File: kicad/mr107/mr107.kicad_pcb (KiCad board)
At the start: 2 copper layers, 35.8 x 70.1 mm, 70 parts, among them J1 USB_A, J10 L-KLS12, J2 gnd, J3 mosi, J4 miso, J5 sclk, J6 reset, J7 gnd, J8 gnd, J9 PW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

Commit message: изменено:      AVR/mr107_/mr107_.ino 	новый файл:    kicad/mr107/bom/ibom.html 	изменено:      kicad/mr107/gerber/Border.gbr 	изменено:      kicad/mr107/gerber/Bottom.gbr 	изменено:      kicad/mr107/gerber/MaskBottom.gbr 	изменено:      kicad/mr107/gerber/MaskTop.gbr 	изменено:      kicad/mr107/gerber/NCData.drl 	изменено:      kicad/mr107/gerber/Top.gbr 	изменено:      kicad/mr107/gerber/mk-gerber.sh 	изменено:      kicad/mr107/gerber/mk-gerber.sh~ 	изменено:      kicad/mr107/gerber/mr107-job.gbrjob 	изменено:      kicad/mr107/gerber/mr107.zip 	удалено:       kicad/mr107/mr107-backups/mr107-2023-12-05_182551.zip 	удалено:       kicad/mr107/mr107-backups/mr107-2023-12-05_183551.zip 	удалено:       kicad/mr107/mr107-backups/mr107-2023-12-05_184551.zip 	удалено:       kicad/mr107/mr107-backups/mr107-2023-12-05_190040.zip 	удалено:       kicad/mr107/mr107-backups/mr107-2023-12-06_163733.zip 	удалено:       kicad/mr107/mr107-backups/mr107-2023-12-06_164916.zip 	удалено:       kicad/mr107/mr107-backups/mr107-2023-12-06_165817.zip 	удалено:       kicad/mr107/mr107-backups/mr107-2023-12-06_185613.zip 	удалено:       kicad/mr107/mr107-backups/mr107-2023-12-06_190115.zip 	удалено:       kicad/mr107/mr107-backups/mr107-2023-12-07_163716.zip 	удалено:       kicad/mr107/mr107-backups/mr107-2023-12-07_164901.zip 	удалено:       kicad/mr107/mr107-backups/mr107-2023-12-10_204652.zip 	удалено:       kicad/mr107/mr107-backups/mr107-2023-12-12_102834.zip 	изменено:      kicad/mr107/mr107.kicad_pcb 	изменено:      kicad/mr107/mr107.kicad_prl 	изменено:      kicad/mr107/mr107.kicad_sch
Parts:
- C1, C10, C17, C7, C9: value C -> 10u
- C11, C12, C13, C14, C21, C22, C28, C6: value C -> 1u
- C29: value 10u -> 1n 2kV
- C8: value .1 -> 10n
- J1: value USB_A -> USBA DS1095B-R

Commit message: изменено:      kicad/mr107/bom/ibom.html 	удалено:       kicad/mr107/gerber/Border.gbr 	удалено:       kicad/mr107/gerber/Bottom.gbr 	удалено:       kicad/mr107/gerber/MaskBottom.gbr 	удалено:       kicad/mr107/gerber/MaskTop.gbr 	удалено:       kicad/mr107/gerber/NCData.drl 	удалено:       kicad/mr107/gerber/Top.gbr 	изменено:      kicad/mr107/gerber/mk-gerber.sh 	удалено:       kicad/mr107/gerber/mk-gerber.sh~ 	удалено:       kicad/mr107/gerber/mr107-job.gbrjob 	изменено:      kicad/mr107/gerber/mr107.zip 	удалено:       kicad/mr107/mr107-backups/mr107-2023-12-07_165931.zip 	удалено:       kicad/mr107/mr107-backups/mr107-2023-12-07_170641.zip 	изменено:      kicad/mr107/mr107.kicad_pcb 	изменено:      kicad/mr107/mr107.kicad_prl 	изменено:      kicad/mr107/mr107.kicad_sch 	удалено:       kicad/mr107_802.3af/mr107-backups/mr107-2023-12-09_164959.zip
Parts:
- C29: footprint Capacitor_SMD:C_0805_2012Metric -> Capacitor_SMD:C_1206_3216Metric
- moved D5 1.50 mm to (60.1, 112.3), turned to 180 degrees
- moved R11 1.06 mm to (73.8, 95.5)
- moved C4 1.05 mm to (63.2, 75.5), turned to 180 degrees
- moved R1 1.03 mm to (72.7, 95.5)
- moved C29 0.55 mm to (85.2, 99.4)
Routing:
- net Net-(D4-Pad3): track 16.4 -> 24.2 mm, vias 3 -> 0
- net Net-(D5-Pad2): track 20.9 -> 14.8 mm, vias 1 -> 0
- net passive_PoE: track 18.5 -> 23.5 mm
- net Net-(D4-Pad1): track 16.4 -> 13.9 mm
- net Net-(D5-Pad1): track 21.8 -> 20.4 mm, vias 1 -> 0
- net GND: vias 13 -> 14

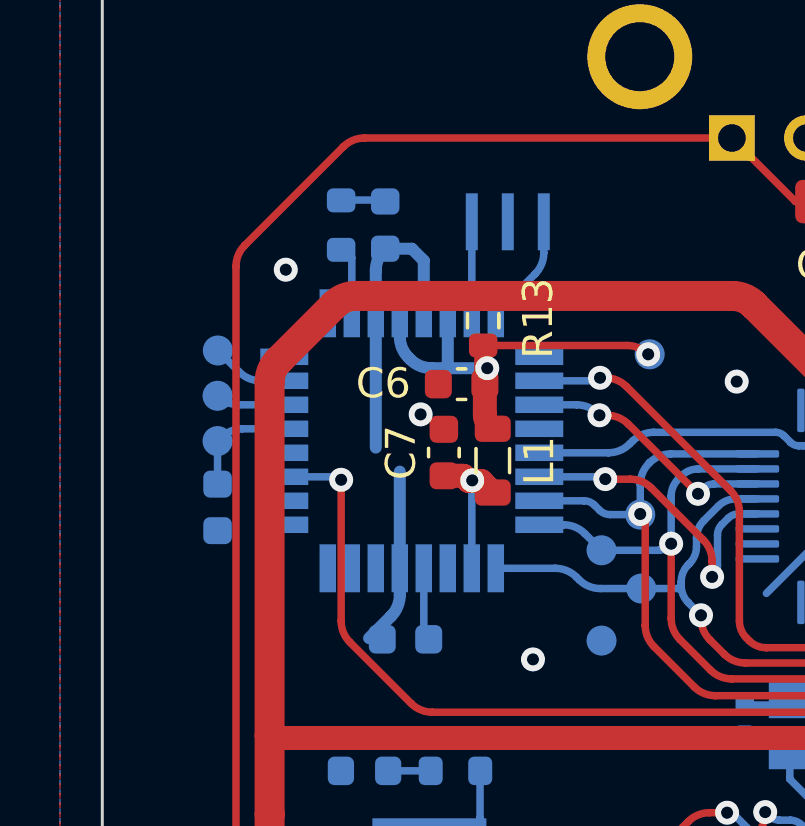
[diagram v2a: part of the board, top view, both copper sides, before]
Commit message: удалено:       kicad/mr107/mr107-backups/mr107-2023-12-12_103509.zip 	удалено:       kicad/mr107/mr107-backups/mr107-2023-12-12_104452.zip 	удалено:       kicad/mr107/mr107-backups/mr107-2023-12-12_105008.zip 	удалено:       kicad/mr107/mr107-backups/mr107-2023-12-12_105739.zip 	изменено:      kicad/mr107/mr107.kicad_pcb 	изменено:      kicad/mr107/mr107.kicad_sch
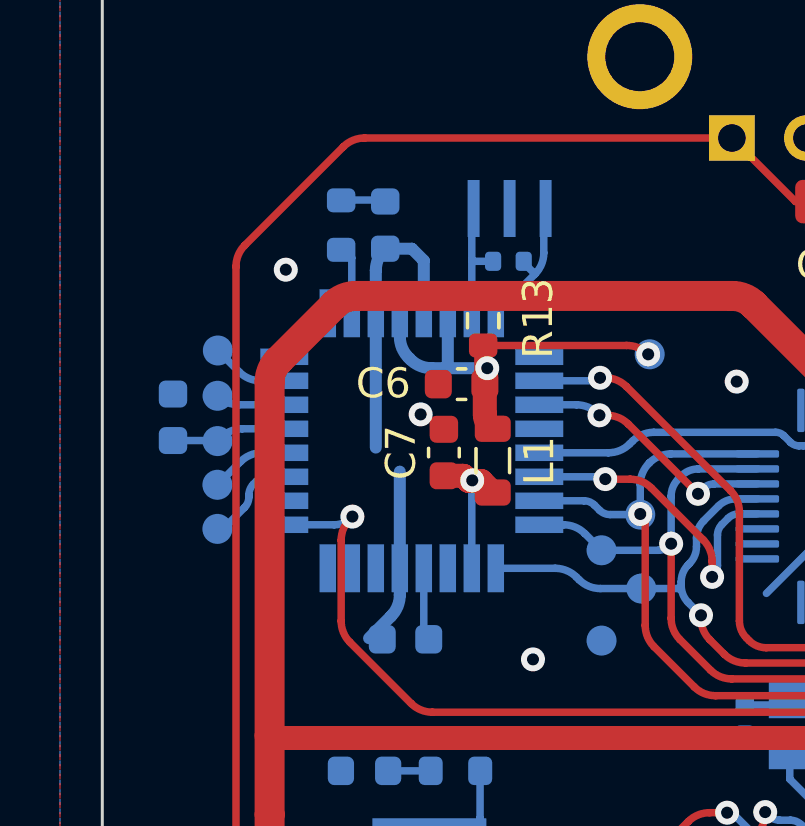
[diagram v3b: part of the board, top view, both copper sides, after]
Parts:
- added J11: mosi, lib:conn_mini, B.Cu at (56.9, 71.8)
- added J12: mosi, lib:conn_mini, B.Cu at (56.9, 70.4)
- added R17: 1M, Resistor_SMD:R_0402_1005Metric, B.Cu at (66.6, 62.9)
- J2: value gnd -> RxD
- J8: value gnd -> TxD
- moved C8 3.35 mm to (55.4, 68.1), turned to 90 degrees
- moved Y3 0.45 mm to (66.7, 61.2)
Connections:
- U2 pad 25: unconnected-(U2-Pad25) -> RST_ETH
- U2 pad 27: RST_ETH -> /sda
- U2 pad 28: unconnected-(U2-Pad28) -> /scl
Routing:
- net /sda: track 0.00 -> 3.16 mm
- net /scl: track 0.00 -> 2.62 mm
- net Net-(U2-Pad7): track 3.05 -> 3.78 mm
- net RST_ETH: track 37.6 -> 36.9 mm
- net Net-(U2-Pad8): track 3.66 -> 4.25 mm

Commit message: изменено:      kicad/mr107/gerber/mr107.zip 	изменено:      kicad/mr107/mr107.kicad_pcb 	изменено:      kicad/mr107/mr107.kicad_sch
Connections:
- U2 pad 25: RST_ETH -> unconnected-(U2-Pad25)
- U2 pad 9: unconnected-(U2-Pad9) -> RST_ETH
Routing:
- net RST_ETH: track 36.9 -> 32.9 mm
- net Net-(C6-Pad1): track 14.6 -> 15.3 mm
- net GND: vias 14 -> 15
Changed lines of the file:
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@@
   (net 54 "Net-(J1-Pad2)")
   (net 55 "Net-(J1-Pad3)")
-  (net 56 "Net-(U2-Pad7)")
-  (net 57 "Net-(U2-Pad8)")
+  (net 56 "Net-(R17-Pad1)")
+  (net 57 "Net-(R17-Pad2)")
   (net 58 "RST")
   (net 59 "Net-(C18-Pad1)")
@@
   (net 90 "/scl")
   (net 91 "Net-(D3-Pad2)")
-  (net 92 "unconnected-(U2-Pad9)")
+  (net 92 "unconnected-(U2-Pad25)")
   (net 93 "unconnected-(D4-Pad5)")
   (net 94 "Net-(D4-Pad9)")
@@
       (net 47 "Net-(C6-Pad1)") (pinfunction "VCC") (pintype "passive"))
     (pad "7" smd rect (at -4.25 -2 270) (size 1.6 0.55) (layers "B.Cu" "B.Paste" "B.Mask")
-      (net 56 "Net-(U2-Pad7)") (pinfunction "XTAL1/PB6") (pintype "bidirectional"))
+      (net 56 "Net-(R17-Pad1)") (pinfunction "XTAL1/PB6") (pintype "bidirectional"))
     (pad "8" smd rect (at -4.25 -2.8 270) (size 1.6 0.55) (layers "B.Cu" "B.Paste" "B.Mask")
-      (net 57 "Net-(U2-Pad8)") (pinfunction "XTAL2/PB7") (pintype "bidirectional"))
+      (net 57 "Net-(R17-Pad2)") (pinfunction "XTAL2/PB7") (pintype "bidirectional"))
     (pad "9" smd rect (at -2.8 -4.25 180) (size 1.6 0.55) (layers "B.Cu" "B.Paste" "B.Mask")
-      (net 92 "unconnected-(U2-Pad9)") (pinfunction "PD5") (pintype "bidirectional+no_connect"))
+      (net 84 "RST_ETH") (pinfunction "PD5") (pintype "bidirectional"))
     (pad "10" smd rect (at -2 -4.25 180) (size 1.6 0.55) (layers "B.Cu" "B.Paste" "B.Mask")
       (net 82 "SS_ETH") (pinfunction "PD6") (pintype "bidirectional"))
@@
       (net 21 "unconnected-(U2-Pad24)") (pinfunction "PC1") (pintype "bidirectional+no_connect"))
     (pad "25" smd rect (at 2.8 4.25 180) (size 1.6 0.55) (layers "B.Cu" "B.Paste" "B.Mask")
-      (net 84 "RST_ETH") (pinfunction "PC2") (pintype "bidirectional"))
+      (net 92 "unconnected-(U2-Pad25)") (pinfunction "PC2") (pintype "bidirectional+no_connect"))
     (pad "26" smd rect (at 2 4.25 180) (size 1.6 0.55) (layers "B.Cu" "B.Paste" "B.Mask")
       (net 23 "unconnected-(U2-Pad26)") (pinfunction "PC3") (pintype "bidirectional+no_connect"))
@@
     (fp_line (start -1.5 -0.3) (end -1.5 0.8) (layer "B.Fab") (width 0.1))
     (pad "1" smd rect (at -1.2 0 180) (size 0.4 1.9) (layers "B.Cu" "B.Paste" "B.Mask")
-      (net 57 "Net-(U2-Pad8)") (pinfunction "1") (pintype "passive"))
+      (net 57 "Net-(R17-Pad2)") (pinfunction "1") (pintype "passive"))
     (pad "2" smd rect (at 0 0 180) (size 0.4 1.9) (layers "B.Cu" "B.Paste" "B.Mask")
       (net 43 "GND") (pinfunction "2") (pintype "passive"))
     (pad "3" smd rect (at 1.2 0 180) (size 0.4 1.9) (layers "B.Cu" "B.Paste" "B.Mask")
-      (net 56 "Net-(U2-Pad7)") (pinfunction "3") (pintype "passive"))
+      (net 56 "Net-(R17-Pad1)") (pinfunction "3") (pintype "passive"))
     (model "${KICAD6_3DMODEL_DIR}/Crystal.3dshapes/Resonator_SMD_Murata_CSTxExxV-3Pin_3.0x1.1mm.wrl"
       (offset (xyz 0 0 0))
@@
     (fp_line (start -0.525 0.27) (end 0.525 0.27) (layer "B.Fab") (width 0.1))
     (pad "1" smd roundrect (at -0.51 0) (size 0.54 0.64) (layers "B.Cu" "B.Paste" "B.Mask") (roundrect_rratio 0.25)
-      (net 56 "Net-(U2-Pad7)") (pintype "passive"))
+      (net 56 "Net-(R17-Pad1)") (pintype "passive"))
     (pad "2" smd roundrect (at 0.51 0) (size 0.54 0.64) (layers "B.Cu" "B.Paste" "B.Mask") (roundrect_rratio 0.25)
-      (net 57 "Net-(U2-Pad8)") (pintype "passive"))
+      (net 57 "Net-(R17-Pad2)") (pintype "passive"))
     (model "${KICAD6_3DMODEL_DIR}/Resistor_SMD.3dshapes/R_0402_1005Metric.wrl"
       (offset (xyz 0 0 0))
@@
   (via (at 71.84 100.88) (size 0.8) (drill 0.4) (layers "F.Cu" "B.Cu") (free) (net 43))
   (via (at 77.02 70.64) (size 0.8) (drill 0.4) (layers "F.Cu" "B.Cu") (net 43))
+  (via (at 74.28 90.89) (size 0.8) (drill 0.4) (layers "F.Cu" "B.Cu") (free) (net 43))
   (via (at 82.33 82.91) (size 0.8) (drill 0.4) (layers "F.Cu" "B.Cu") (free) (net 43))
   (via (at 66.51 86.92) (size 0.8) (drill 0.4) (layers "F.Cu" "B.Cu") (free) (net 43))
@@
   (segment (start 78.56 80.68) (end 78.56 79.55) (width 0.25) (layer "B.Cu") (net 46))
   (segment (start 65.77 65.735) (end 65.77 66.97) (width 0.6) (layer "F.Cu") (net 47))
-  (segment (start 65.77 65.735) (end 70.560786 65.735) (width 0.25) (layer "F.Cu") (net 47))
+  (segment (start 70.015786 65) (end 66.919214 65) (width 0.25) (layer "F.Cu") (net 47))
+  (segment (start 66.212107 65.292893) (end 65.77 65.735) (width 0.25) (layer "F.Cu") (net 47))
+  (segment (start 71.27 65.84) (end 70.722893 65.292893) (width 0.25) (layer "F.Cu") (net 47))
+  (segment (start 71.27 66.03) (end 71.27 65.84) (width 0.25) (layer "F.Cu") (net 47))
   (segment (start 65.825 67.025) (end 65.825 68.040393) (width 0.8) (layer "F.Cu") (net 47))
   (segment (start 65.77 66.97) (end 65.825 67.025) (width 0.25) (layer "F.Cu") (net 47))
@@
   (via (at 65.905 66.493) (size 0.8) (drill 0.4) (layers "F.Cu" "B.Cu") (net 47))
   (via (at 71.27 66.03) (size 0.8) (drill 0.4) (layers "F.Cu" "B.Cu") (net 47))
-  (arc (start 70.560786 65.735) (mid 70.943469 65.81112) (end 71.267893 66.027893) (width 0.25) (layer "F.Cu") (net 47))
+  (arc (start 70.722893 65.292893) (mid 70.39847 65.07612) (end 70.015786 65) (width 0.25) (layer "F.Cu") (net 47))
+  (arc (start 66.212107 65.292893) (mid 66.53653 65.07612) (end 66.919214 65) (width 0.25) (layer "F.Cu") (net 47))
   (arc (start 65.971447 68.393947) (mid 65.86306 68.231735) (end 65.825 68.040393) (width 0.8) (layer "F.Cu") (net 47))
   (segment (start 64.555 66.493) (end 65.905 66.493) (width 0.4) (layer "B.Cu") (net 47))
@@
   (segment (start 79.201447 81.088553) (end 84.48 75.81) (width 0.25) (layer "B.Cu") (net 82))
   (arc (start 79.055 81.442107) (mid 79.09306 81.250765) (end 79.201447 81.088553) (width 0.25) (layer "B.Cu") (net 82))
-  (segment (start 84.49 80.32) (end 82.422893 78.252893) (width 0.25) (layer "F.Cu") (net 84))
-  (segment (start 81.715786 77.96) (end 64.074214 77.96) (width 0.25) (layer "F.Cu") (net 84))
-  (segment (start 63.367107 77.667107) (end 61.327893 75.627893) (width 0.25) (layer "F.Cu") (net 84))
-  (segment (start 61.035 74.920786) (end 61.035 72.229214) (width 0.25) (layer "F.Cu") (net 84))
-  (segment (start 61.327893 71.522107) (end 61.41 71.44) (width 0.25) (layer "F.Cu") (net 84))
+  (segment (start 73.164214 77.96) (end 81.715786 77.96) (width 0.25) (layer "F.Cu") (net 84))
+  (segment (start 68.98 65.86) (end 68.8 66.04) (width 0.25) (layer "F.Cu") (net 84))
+  (segment (start 68.8 66.04) (end 68.8 70.045786) (width 0.25) (layer "F.Cu") (net 84))
+  (segment (start 69.092893 70.752893) (end 70.237107 71.897107) (width 0.25) (layer "F.Cu") (net 84))
+  (segment (start 70.53 72.604214) (end 70.53 75.325786) (width 0.25) (layer "F.Cu") (net 84))
+  (segment (start 82.422893 78.252893) (end 84.49 80.32) (width 0.25) (layer "F.Cu") (net 84))
+  (segment (start 70.822893 76.032893) (end 72.457107 77.667107) (width 0.25) (layer "F.Cu") (net 84))
   (via (at 84.49 80.32) (size 0.8) (drill 0.4) (layers "F.Cu" "B.Cu") (free) (net 84))
-  (via (at 61.41 71.44) (size 0.8) (drill 0.4) (layers "F.Cu" "B.Cu") (free) (net 84))
-  (arc (start 61.327893 71.522107) (mid 61.11112 71.84653) (end 61.035 72.229214) (width 0.25) (layer "F.Cu") (net 84))
-  (arc (start 61.327893 75.627893) (mid 61.11112 75.303469) (end 61.035 74.920786) (width 0.25) (layer "F.Cu") (net 84))
-  (arc (start 64.074214 77.96) (mid 63.691531 77.88388) (end 63.367107 77.667107) (width 0.25) (layer "F.Cu") (net 84))
-  (arc (start 82.422893 78.252893) (mid 82.09847 78.03612) (end 81.715786 77.96) (width 0.25) (layer "F.Cu") (net 84))
+  (via (at 68.98 65.86) (size 0.8) (drill 0.4) (layers "F.Cu" "B.Cu") (free) (net 84))
+  (arc (start 69.092893 70.752893) (mid 68.87612 70.42847) (end 68.8 70.045786) (width 0.25) (layer "F.Cu") (net 84))
+  (arc (start 70.237107 71.897107) (mid 70.45388 72.22153) (end 70.53 72.604214) (width 0.25) (layer "F.Cu") (net 84))
+  (arc (start 73.164214 77.96) (mid 72.781531 77.88388) (end 72.457107 77.667107) (width 0.25) (layer "F.Cu") (net 84))
+  (arc (start 70.53 75.325786) (mid 70.60612 75.708469) (end 70.822893 76.032893) (width 0.25) (layer "F.Cu") (net 84))
+  (arc (start 81.715786 77.96) (mid 82.09847 78.03612) (end 82.422893 78.252893) (width 0.25) (layer "F.Cu") (net 84))
   (segment (start 84.49 82.775786) (end 84.49 80.32) (width 0.25) (layer "B.Cu") (net 84))
-  (segment (start 59.14 71.713) (end 60.805629 71.713) (width 0.25) (layer "B.Cu") (net 84))
+  (segment (start 67.64 66.113) (end 68.519893 66.113) (width 0.25) (layer "B.Cu") (net 84))
   (segment (start 82.4675 84.184214) (end 83.081572 84.184214) (width 0.25) (layer "B.Cu") (net 84))
-  (segment (start 61.371315 71.478685) (end 61.41 71.44) (width 0.25) (layer "B.Cu") (net 84))
   (segment (start 83.788679 83.891321) (end 84.197107 83.482893) (width 0.25) (layer "B.Cu") (net 84))
-  (arc (start 60.805629 71.713) (mid 61.111776 71.652103) (end 61.371315 71.478685) (width 0.25) (layer "B.Cu") (net 84))
+  (segment (start 68.873447 65.966553) (end 68.98 65.86) (width 0.25) (layer "B.Cu") (net 84))
+  (arc (start 68.873447 65.966553) (mid 68.711235 66.07494) (end 68.519893 66.113) (width 0.25) (layer "B.Cu") (net 84))
   (arc (start 83.788679 83.891321) (mid 83.464256 84.108094) (end 83.081572 84.184214) (width 0.25) (layer "B.Cu") (net 84))
   (arc (start 84.197107 83.482893) (mid 84.41388 83.15847) (end 84.49 82.775786) (width 0.25) (layer "B.Cu") (net 84))

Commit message: изменено:      kicad/mr107/fp-info-cache 	изменено:      kicad/mr107/mr107.kicad_pcb 	изменено:      kicad/mr107/mr107.kicad_prl 	изменено:      kicad/mr107/mr107.kicad_sch
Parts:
- moved J9 0.89 mm to (71.9, 65.3)
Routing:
- net GND: track 60.7 -> 101.8 mm, vias 15 -> 18
- net Net-(C19-Pad1): track 6.67 -> 5.18 mm
- net SS_ETH: track 32.2 -> 30.9 mm
- net MOSI: track 33.7 -> 32.9 mm
